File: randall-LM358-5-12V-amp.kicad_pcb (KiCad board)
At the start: 2 copper layers, 100.3 x 77.5 mm, 27 parts, among them J1 Power, Q1 TIP120, Q2 TIP120, U1 LM2674M-3.3, U2 LM358, U3 Z-Uno

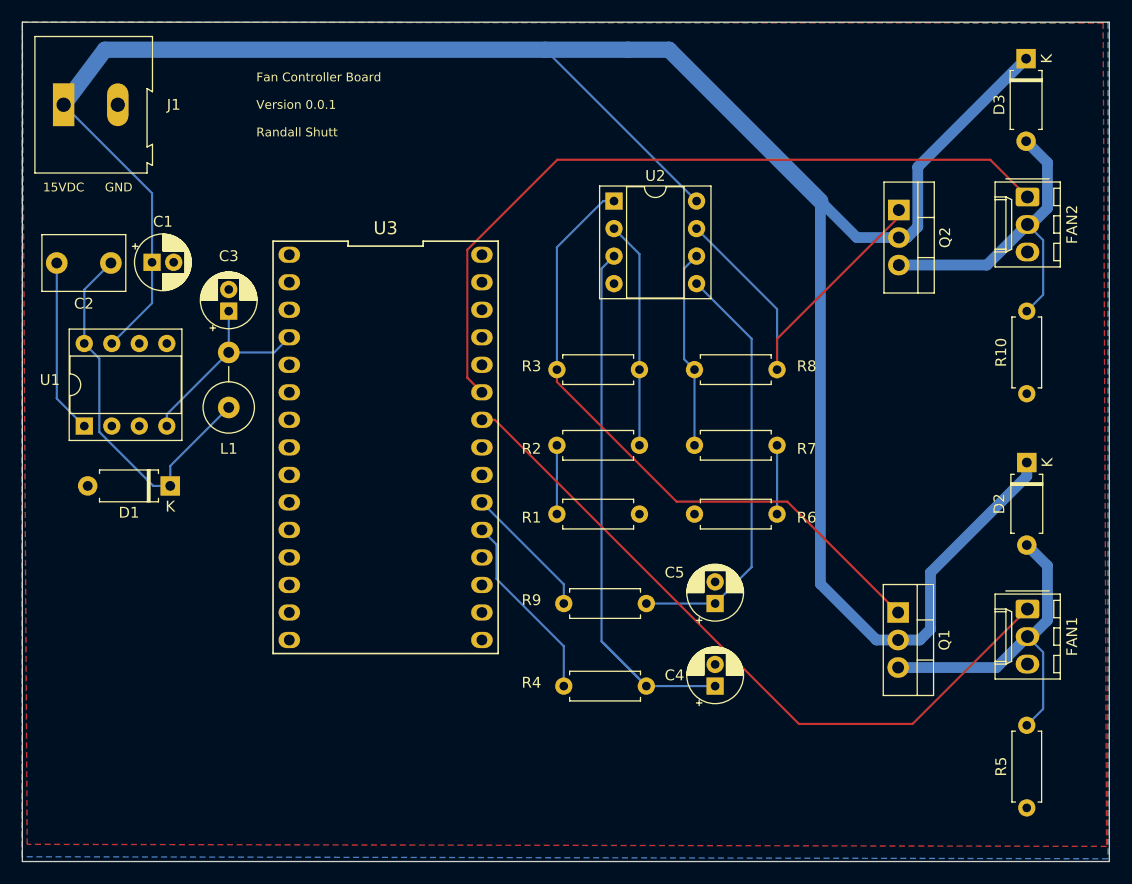
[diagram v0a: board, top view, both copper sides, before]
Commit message: Updated with P/Ns where necessary
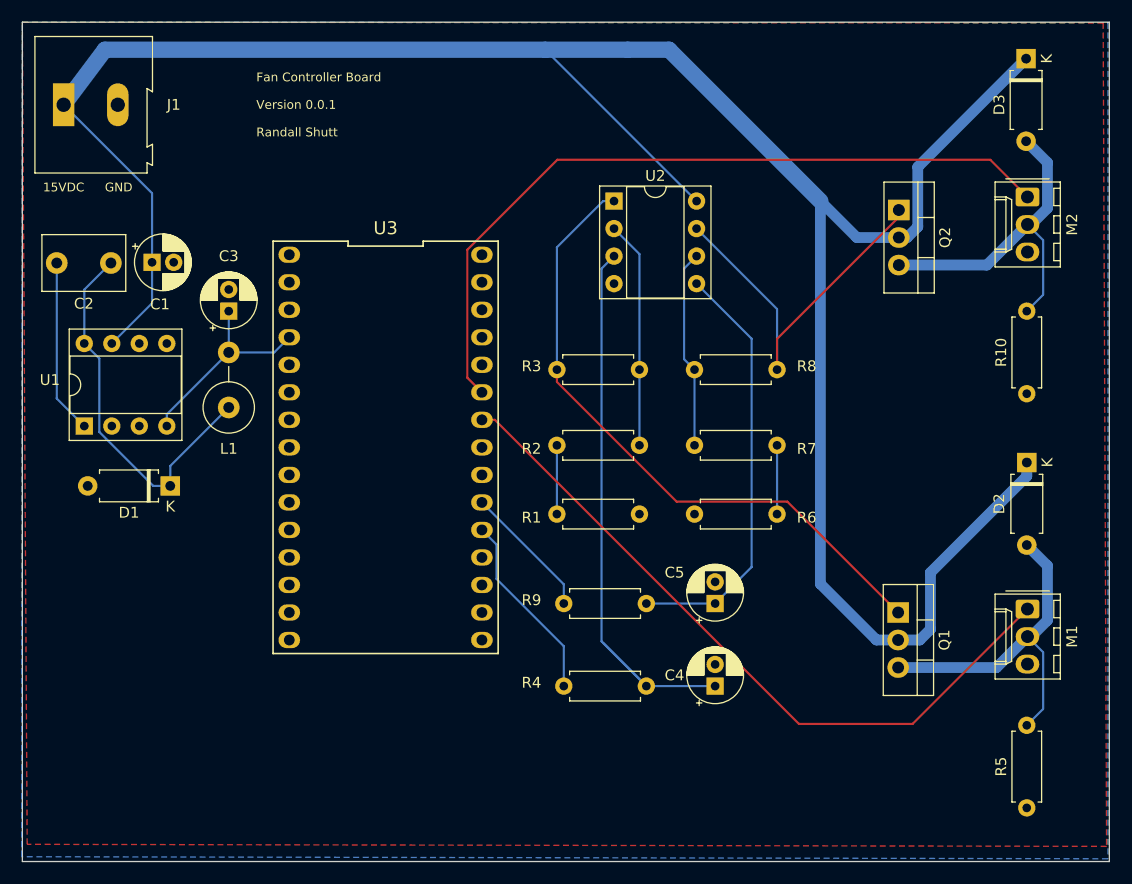
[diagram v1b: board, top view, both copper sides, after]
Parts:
- C1, C3: value 100uF -> 100uF OSCON-SEP
- C4, C5: value 100uF -> 100uF 25v
- D1: value D_Schottky -> 11DQ05TA
- D2, D3: value 1N1004 -> 1N4004G-T
- J1: value Power -> Barrel_Jack
- L1: value 68uH -> 68uH B78148E
- M1: renamed from FAN1; value Fan_3pin -> Molex 22292031
- M2: renamed from FAN2; value Fan_3pin -> Molex 22292031
- R10, R5: value 46k -> 47k
- U1: value LM2674M-3.3 -> LM2674N-3.3/NOPB
- U2: value LM358 -> LM358N/NOPB
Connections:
- U1 pad 2: (no net) -> Net-(U1-Pad2)
- U1 pad 3: (no net) -> Net-(U1-Pad3)
- U1 pad 5: (no net) -> Net-(U1-Pad5)
- U3 pad 1: (no net) -> Net-(U3-Pad1)
- U3 pad 10: (no net) -> Net-(U3-Pad10)
- U3 pad 11: (no net) -> Net-(U3-Pad11)
- U3 pad 12: (no net) -> Net-(U3-Pad12)
- U3 pad 13: (no net) -> Net-(U3-Pad13)
- U3 pad 14: (no net) -> Net-(U3-Pad14)
- U3 pad 15: (no net) -> Net-(U3-Pad15)
- U3 pad 16: (no net) -> Net-(U3-Pad16)
- U3 pad 17: (no net) -> Net-(U3-Pad17)
- U3 pad 18: (no net) -> Net-(U3-Pad18)
- U3 pad 19: (no net) -> Net-(U3-Pad19)
- U3 pad 2: (no net) -> Net-(U3-Pad2)
- U3 pad 22: (no net) -> Net-(U3-Pad22)
- U3 pad 23: (no net) -> Net-(U3-Pad23)
- U3 pad 26: (no net) -> Net-(U3-Pad26)
- U3 pad 27: (no net) -> Net-(U3-Pad27)
- U3 pad 28: (no net) -> Net-(U3-Pad28)
- U3 pad 5: (no net) -> Net-(U3-Pad5)
- U3 pad 6: (no net) -> Net-(U3-Pad6)
- U3 pad 7: (no net) -> Net-(U3-Pad7)
- U3 pad 8: (no net) -> Net-(U3-Pad8)
- U3 pad 9: (no net) -> Net-(U3-Pad9)
